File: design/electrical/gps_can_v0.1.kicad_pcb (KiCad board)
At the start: 2 copper layers, 90.2 x 95.9 mm, 21 parts, among them IC1 ATMEGA16M1-A, J1 SMA, U1 TPS2030, U2 LM1117-3.3, U3 RXM-GPS-RM, U4 ADG787, U5 ATA6561, U6 ATA6561

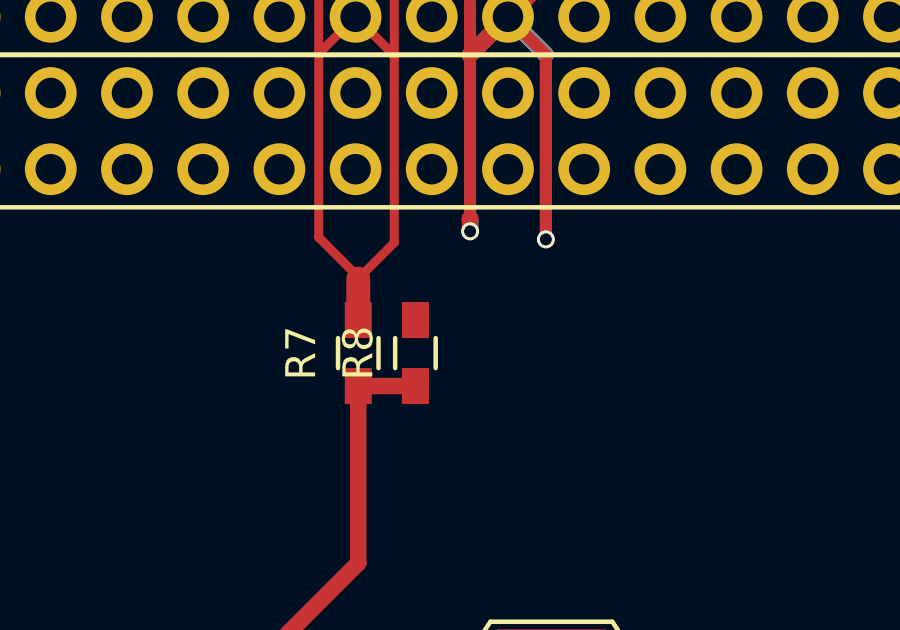
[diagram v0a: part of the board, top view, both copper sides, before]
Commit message: Added pad for alternative +5V supply.
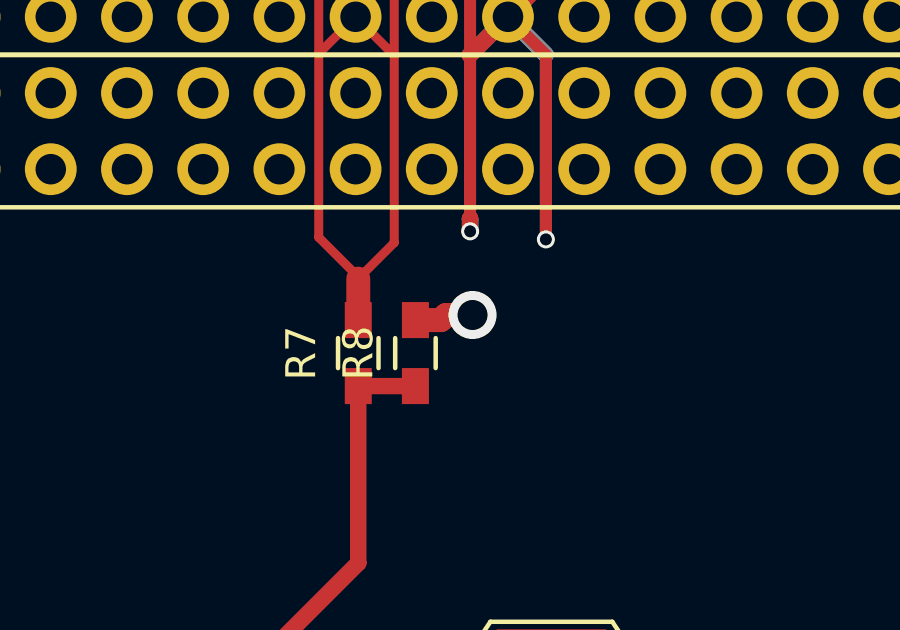
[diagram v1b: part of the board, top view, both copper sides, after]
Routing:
- net ALT_5V: track 0.00 -> 1.98 mm, vias 0 -> 1
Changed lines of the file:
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@@
     (thickness 1.6)
     (drawings 1584)
-    (tracks 380)
+    (tracks 384)
     (zones 0)
     (modules 21)
@@
   (segment (start 81.02 87.255) (end 81.02 89.8) (width 0.55) (layer F.Cu) (net 140))
   (segment (start 103.971822 86.552596) (end 81.722404 86.552596) (width 0.55) (layer F.Cu) (net 140))
+  (via (at 113.03 69.85) (size 1.6) (drill 1) (layers F.Cu B.Cu) (net 141))
+  (segment (start 112.145 69.85) (end 113.03 69.85) (width 0.8) (layer F.Cu) (net 141))
+  (segment (start 111.125 70.02) (end 111.975 70.02) (width 0.8) (layer F.Cu) (net 141))
+  (segment (start 111.975 70.02) (end 112.145 69.85) (width 0.8) (layer F.Cu) (net 141))
   (zone (net 2) (net_name GND) (layer F.Cu) (hatch edge 0.508)
     (connect_pads (clearance 0.508))
